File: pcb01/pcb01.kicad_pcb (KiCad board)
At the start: 2 copper layers, 118.1 x 98.4 mm, 53 parts, among them J1 DIN41612_02x32_AC, J10 Conn_01x02_Socket, J11 Conn_01x09, J4 Display, J5 UART, J6 UART_IRQ, J7 Jmp_Irq, J8 Jmp_NMI, J9 Ram1 Enable, SW1 SW_Push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

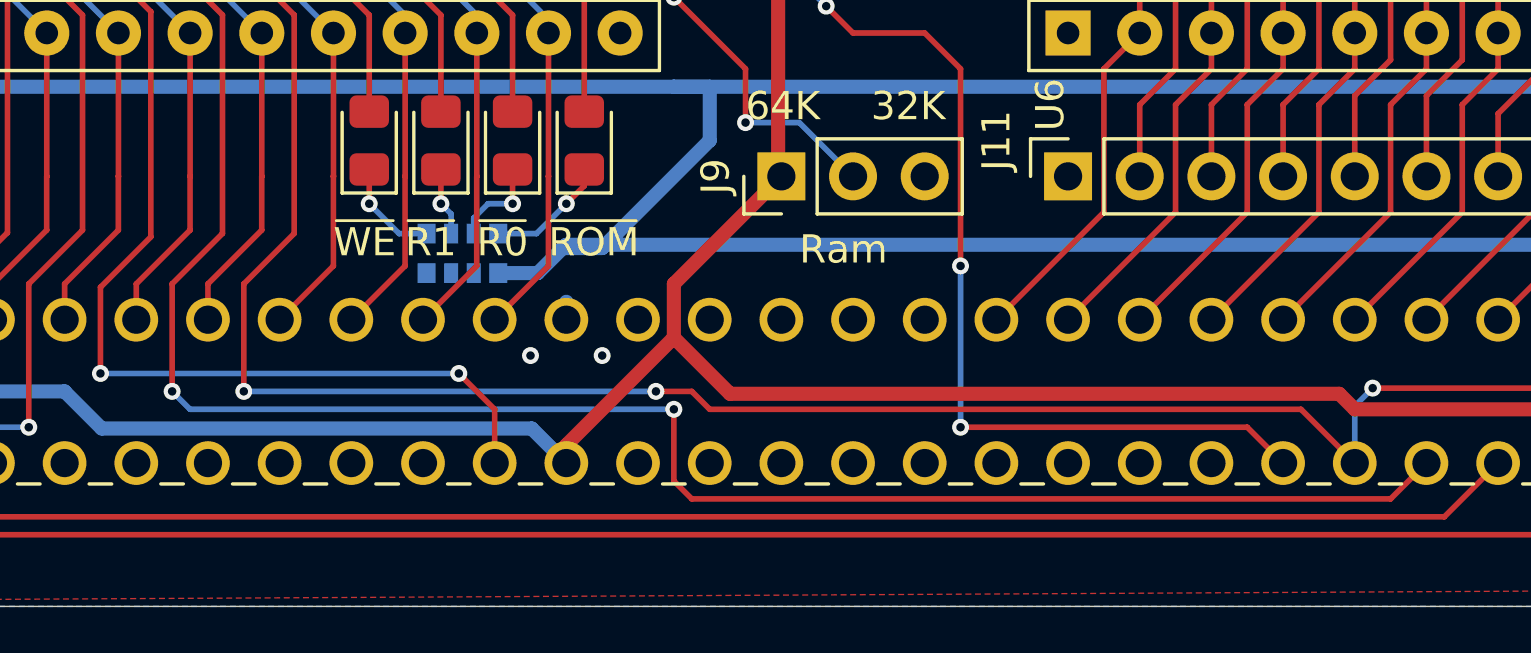
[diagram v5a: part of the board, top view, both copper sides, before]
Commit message: small power routing fix
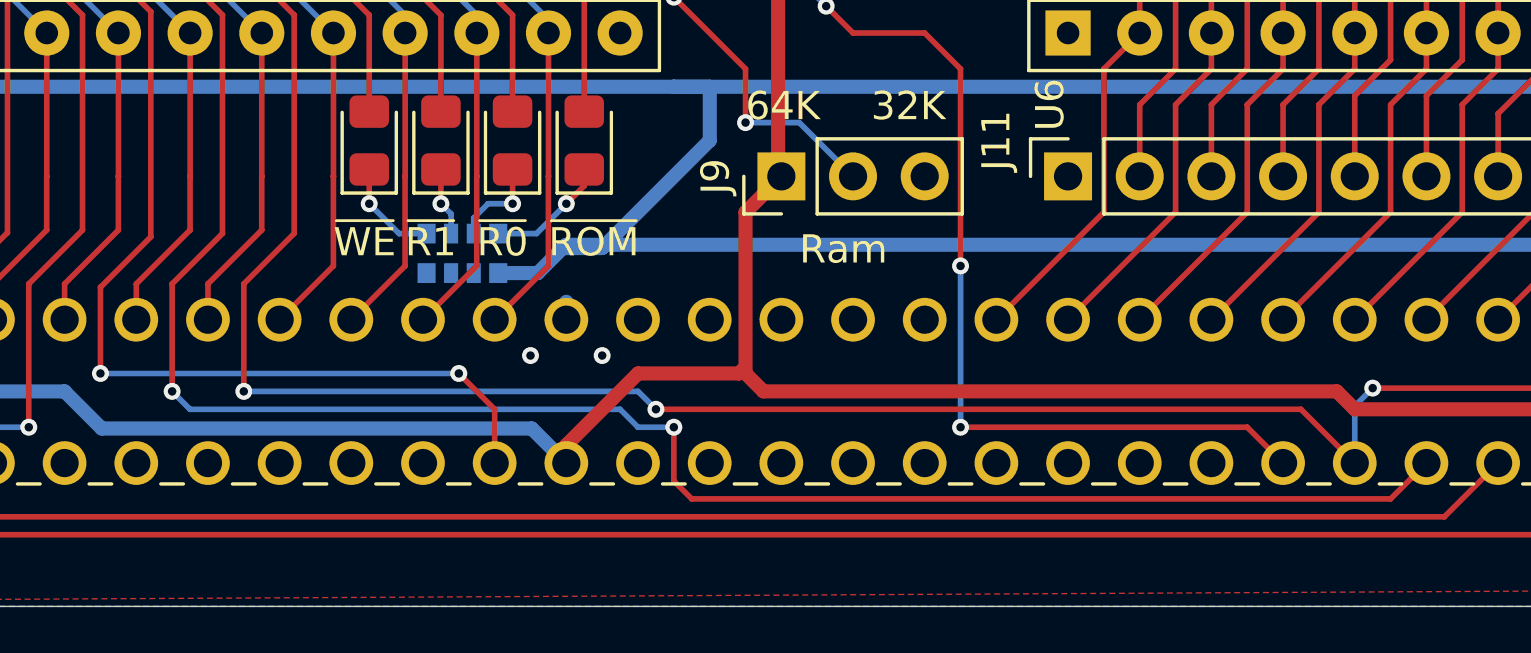
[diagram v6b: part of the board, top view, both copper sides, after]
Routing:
- net VCC: track 511.5 -> 510.8 mm
